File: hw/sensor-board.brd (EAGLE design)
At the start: 50 x 40 mm, 51 parts, among them U1 LT1762EMS8-3.3PBF, U2 ULN2003LVPWR, U3 ULN2003LVPWR, U4 PCA9685PW, U5 AT42QT1070-SSU, X1 MOLEX-501953-0407, X2 MOLEX-501953-0407

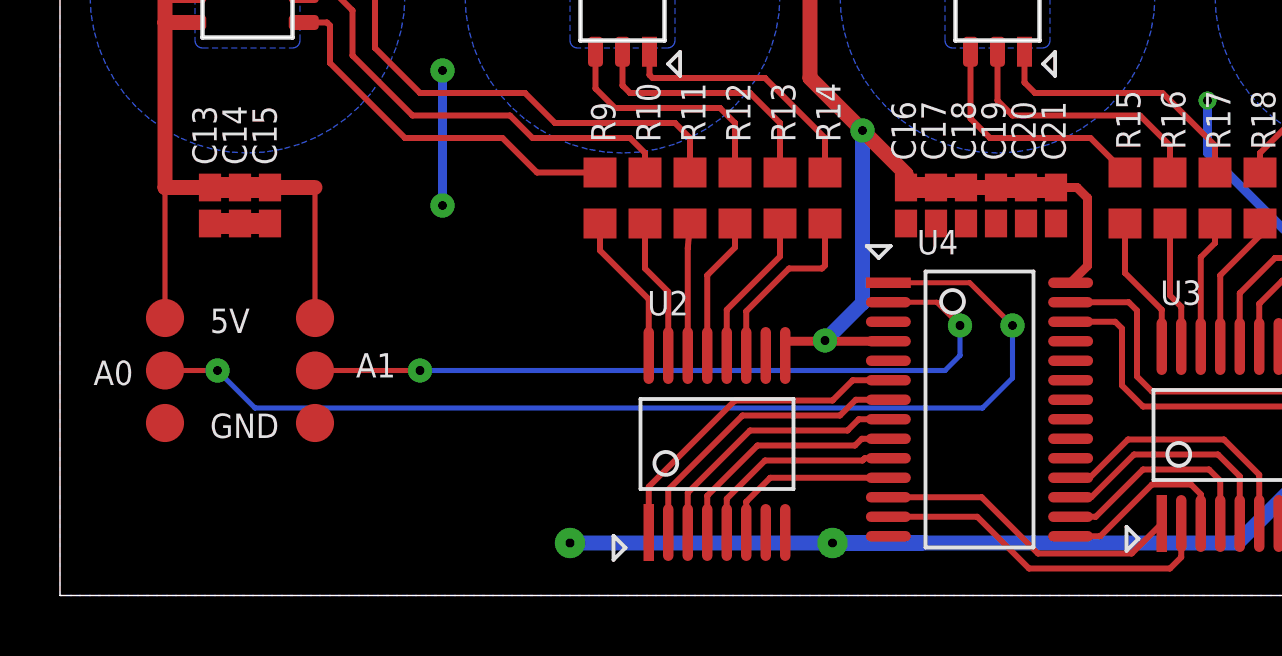
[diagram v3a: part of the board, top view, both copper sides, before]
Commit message: Switched VDD of LED PWM driver to 3.3V.
Added an LDO to generate VDD for LED PWM driver.
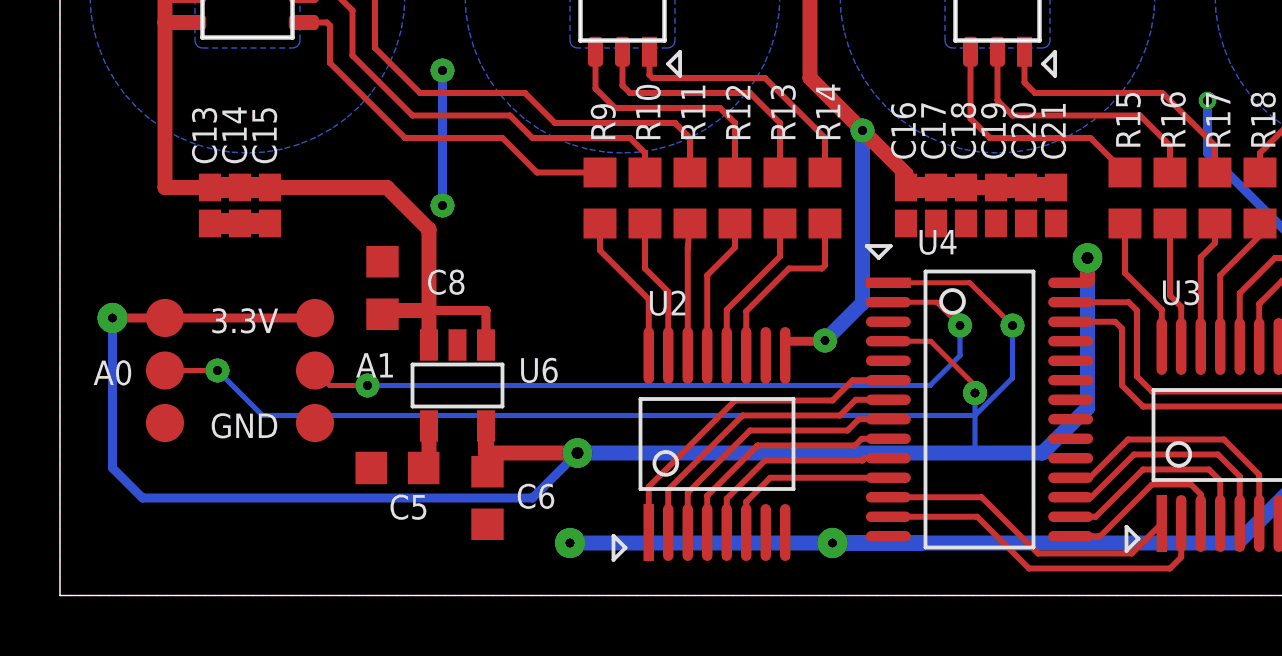
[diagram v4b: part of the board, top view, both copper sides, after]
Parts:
- added C5: 0.01uF 25V, rcl:C0603K
- added C6, C8: 1uF 25V, rcl:C0603K
- added U6: TPS730XX, vreg:SOT23-5
- renumbered 5V to 3.3V
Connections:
- new net N$1: C5.1, U6.4
- new net N$9: 3.3V.TP, C6.2, TP1.TP, U4.28, U4.4, U6.5
- net GND: now also C5.2, C6.1, C8.2, U2.7, U3.7, U6.2
- net VDD_5: now also C8.1, U6.1, U6.3; no longer 3.3V.TP, TP1.TP, U4.28, U4.4
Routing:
- net N$9: track 0.00 -> 65.8 mm, vias 0 -> 4
- net VDD_5: track 150.3 -> 148.1 mm
- net N$1: track 0.00 -> 1.58 mm
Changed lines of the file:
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@@
 <attribute name="VALUE" x="4.262" y="8.615" size="0.0254" layer="27" rot="R90"/>
 </element>
-<element name="5V" library="testpad" package="B1,27" value="TPB1,27" x="8.5" y="9.25" smashed="yes" rot="R90">
+<element name="3.3V" library="testpad" package="B1,27" value="TPB1,27" x="8.5" y="9.25" smashed="yes" rot="R90">
 <attribute name="TP_SIGNAL_NAME" value="" x="10.405" y="8.615" size="1" layer="37" rot="R90"/>
 <attribute name="NAME" x="5" y="8.75" size="0.8128" layer="25" font="vector" ratio="10"/>
@@
 <attribute name="ELEMENT14_URL" value="http://sg.element14.com/jsp/search/productdetail.jsp?sku=1799462" x="10" y="29.25" size="0.8128" layer="27" display="off"/>
 <attribute name="MFR_PART" value="RC0603JR-1047KL" x="10" y="29.25" size="0.8128" layer="27" display="off"/>
+</element>
+<element name="U6" library="vreg" package="SOT23-5" value="TPS730XX" x="13.25" y="7" smashed="yes" rot="R180">
+<attribute name="NAME" x="16.655" y="7.91" size="0.8128" layer="25" rot="R180"/>
+<attribute name="VALUE" x="15.155" y="10.175" size="0.8128" layer="27" rot="R180"/>
+</element>
+<element name="C5" library="rcl" package="C0603K" value="0.01uF 25V" x="11.25" y="4.25" smashed="yes" rot="R180">
+<attribute name="ELEMENT14_URL" value="http://sg.element14.com/jsp/search/productdetail.jsp?sku=1692285" x="11.25" y="4.25" size="0.8128" layer="27" rot="R180" display="off"/>
+<attribute name="MFR_PART" value="C0402C103J3RACTU" x="11.25" y="4.25" size="0.8128" layer="27" rot="R180" display="off"/>
+<attribute name="NAME" x="12.3" y="3.35" size="0.8128" layer="25" rot="R180"/>
+<attribute name="VALUE" x="12.05" y="5.9" size="1.016" layer="27" rot="R180"/>
+</element>
+<element name="C6" library="rcl" package="C0603K" value="1uF 25V" x="14.25" y="3.25" smashed="yes" rot="R90">
+<attribute name="ELEMENT14_URL" value="http://sg.element14.com/jsp/search/productdetail.jsp?sku=2146156" x="14.25" y="3.25" size="0.8128" layer="27" rot="R90" display="off"/>
+<attribute name="MFR_PART" value="C1608X7R1C105K080AC" x="14.25" y="3.25" size="0.8128" layer="27" rot="R90" display="off"/>
+<attribute name="NAME" x="15.2" y="2.9" size="0.8128" layer="25"/>
+<attribute name="VALUE" x="15.9" y="2.45" size="1.016" layer="27" rot="R90"/>
+</element>
+<element name="C8" library="rcl" package="C0603K" value="1uF 25V" x="10.75" y="10.25" smashed="yes" rot="R90">
+<attribute name="ELEMENT14_URL" value="http://sg.element14.com/jsp/search/productdetail.jsp?sku=2146156" x="10.75" y="10.25" size="0.8128" layer="27" rot="R90" display="off"/>
+<attribute name="MFR_PART" value="C1608X7R1C105K080AC" x="10.75" y="10.25" size="0.8128" layer="27" rot="R90" display="off"/>
+<attribute name="NAME" x="13.55" y="10.85" size="0.8128" layer="25" rot="R180"/>
+<attribute name="VALUE" x="12.4" y="9.45" size="1.016" layer="27" rot="R90"/>
 </element>
 </elements>
@@
 <contactref element="U1" pad="8"/>
 <contactref element="C3" pad="1"/>
-<contactref element="U4" pad="28"/>
 <contactref element="C13" pad="2"/>
 <contactref element="X2" pad="1"/>
@@
 <wire x1="44.5" y1="13.6" x2="45.5" y2="13.6" width="0.5" layer="1"/>
 <wire x1="45.5" y1="13.6" x2="46.5" y2="13.6" width="0.5" layer="1"/>
-<contactref element="U4" pad="4"/>
-<wire x1="27.6125" y1="8.475" x2="25.475" y2="8.475" width="0.3" layer="1"/>
 <wire x1="24.175" y1="8.475" x2="24.175" y2="8" width="0.2" layer="1"/>
 <wire x1="12.9" y1="31.025" x2="13.775" y2="31.025" width="0.3" layer="1"/>
@@
 <wire x1="13.75" y1="34.25" x2="12.9" y2="33.4" width="0.3" layer="1"/>
 <contactref element="X1" pad="1"/>
-<contactref element="TP1" pad="TP"/>
-<contactref element="5V" pad="TP"/>
 <wire x1="47.75" y1="22.75" x2="47.75" y2="13.5" width="0.5" layer="1"/>
 <wire x1="47.75" y1="13.5" x2="47.75" y2="11.75" width="0.5" layer="1"/>
@@
 <wire x1="24.175" y1="8.475" x2="25.475" y2="8.475" width="0.3" layer="1"/>
 <wire x1="25.475" y1="8.475" x2="25.5" y2="8.5" width="0.3" layer="1"/>
-<wire x1="33.2" y1="13.6" x2="33.9" y2="13.6" width="0.3" layer="1"/>
-<wire x1="33.9" y1="13.6" x2="34.25" y2="13.25" width="0.3" layer="1"/>
-<wire x1="34.25" y1="13.25" x2="34.25" y2="10.9875" width="0.3" layer="1"/>
-<wire x1="34.25" y1="10.9875" x2="33.6875" y2="10.425" width="0.3" layer="1"/>
-<wire x1="3.5" y1="13.6" x2="3.5" y2="9.25" width="0.17" layer="1"/>
-<wire x1="8.5" y1="9.25" x2="8.5" y2="13.6" width="0.17" layer="1"/>
 <wire x1="3.5" y1="13.6" x2="5" y2="13.6" width="0.5" layer="1"/>
-<wire x1="8.5" y1="13.6" x2="7" y2="13.6" width="0.5" layer="1"/>
 <wire x1="25" y1="17.25" x2="25" y2="22.75" width="0.5" layer="1"/>
+<contactref element="U6" pad="1"/>
+<contactref element="U6" pad="3"/>
+<wire x1="7" y1="13.6" x2="10.9" y2="13.6" width="0.5" layer="1"/>
+<wire x1="10.9" y1="13.6" x2="12.3" y2="12.2" width="0.5" layer="1"/>
+<wire x1="12.3" y1="12.2" x2="12.3" y2="9.5" width="0.5" layer="1"/>
+<wire x1="12.3" y1="9.5" x2="12.3" y2="8.35" width="0.5" layer="1"/>
+<wire x1="14.2" y1="8.35" x2="14.2" y2="9.5" width="0.3048" layer="1"/>
+<wire x1="14.2" y1="9.5" x2="12.3" y2="9.5" width="0.3048" layer="1"/>
+<contactref element="C8" pad="1"/>
+<wire x1="10.75" y1="9.375" x2="10.75" y2="9.5" width="0.5" layer="1"/>
+<wire x1="10.75" y1="9.5" x2="12.3" y2="9.5" width="0.5" layer="1"/>
 <wire x1="18" y1="22.75" x2="13.775" y2="31.025" width="0" layer="19" extent="1-1"/>
 </signal>
@@
 <contactref element="X2" pad="5"/>
 <contactref element="PWR" pad="2"/>
+<contactref element="U6" pad="2"/>
+<contactref element="C5" pad="2"/>
+<contactref element="C6" pad="1"/>
+<contactref element="U2" pad="7"/>
+<contactref element="U3" pad="7"/>
+<contactref element="C8" pad="2"/>
 </signal>
 <signal name="VDD_3_3">
@@
 <via x="31.75" y="9" extent="1-16" drill="0.3" diameter="0.8128"/>
 <wire x1="31.75" y1="9" x2="31.75" y2="7.25" width="0.17" layer="16"/>
-<wire x1="31.75" y1="7.25" x2="30.75" y2="6.25" width="0.17" layer="16"/>
-<wire x1="30.75" y1="6.25" x2="6.5" y2="6.25" width="0.17" layer="16"/>
-<wire x1="6.5" y1="6.25" x2="5.25" y2="7.5" width="0.17" layer="16"/>
 <via x="5.25" y="7.5" extent="1-16" drill="0.3" diameter="0.8128"/>
+<wire x1="31.75" y1="7.25" x2="30.5" y2="6" width="0.17" layer="16"/>
+<wire x1="30.5" y1="6" x2="6.75" y2="6" width="0.17" layer="16"/>
+<wire x1="6.75" y1="6" x2="5.25" y2="7.5" width="0.17" layer="16"/>
 </signal>
 <signal name="N$7">
@@
 <wire x1="29.225" y1="9.775" x2="30" y2="9" width="0.17" layer="1"/>
 <via x="30" y="9" extent="1-16" drill="0.3" diameter="0.8128"/>
-<wire x1="30" y1="9" x2="30" y2="8" width="0.17" layer="16"/>
-<wire x1="30" y1="8" x2="29.5" y2="7.5" width="0.17" layer="16"/>
-<wire x1="29.5" y1="7.5" x2="12" y2="7.5" width="0.17" layer="16"/>
-<via x="12" y="7.5" extent="1-16" drill="0.3" diameter="0.8128"/>
-<wire x1="12" y1="7.5" x2="8.5" y2="7.5" width="0.17" layer="1"/>
+<via x="10.25" y="7" extent="1-16" drill="0.3" diameter="0.8128"/>
+<wire x1="10.25" y1="7" x2="29" y2="7" width="0.17" layer="16"/>
+<wire x1="29" y1="7" x2="30" y2="8" width="0.17" layer="16"/>
+<wire x1="30" y1="8" x2="30" y2="9" width="0.17" layer="16"/>
+<wire x1="10.25" y1="7" x2="9" y2="7" width="0.17" layer="1"/>
+<wire x1="9" y1="7" x2="8.5" y2="7.5" width="0.17" layer="1"/>
+</signal>
+<signal name="N$9">
+<contactref element="U4" pad="4"/>
+<contactref element="U4" pad="28"/>
+<contactref element="U6" pad="5"/>
+<contactref element="TP1" pad="TP"/>
+<contactref element="3.3V" pad="TP"/>
+<contactref element="C6" pad="2"/>
+<wire x1="14.2" y1="5.65" x2="14.2" y2="4.125" width="0.5" layer="1"/>
+<wire x1="14.2" y1="4.125" x2="14.25" y2="4.125" width="0.5" layer="1"/>
+<wire x1="14.2" y1="5.65" x2="14.2" y2="4.75" width="0.5" layer="1"/>
+<wire x1="14.2" y1="4.75" x2="17.25" y2="4.75" width="0.5" layer="1"/>
+<via x="17.25" y="4.75" extent="1-16" drill="0.4" diameter="1"/>
+<wire x1="17.25" y1="4.75" x2="32.75" y2="4.75" width="0.5" layer="16"/>
+<wire x1="32.75" y1="4.75" x2="34.25" y2="6.25" width="0.5" layer="16"/>
+<wire x1="34.25" y1="6.25" x2="34.25" y2="11.25" width="0.5" layer="16"/>
+<via x="34.25" y="11.25" extent="1-16" drill="0.4" diameter="1"/>
+<wire x1="34.25" y1="11.25" x2="34.25" y2="10.5" width="0.5" layer="1"/>
+<wire x1="34.25" y1="10.5" x2="34.175" y2="10.425" width="0.3" layer="1"/>
+<wire x1="34.175" y1="10.425" x2="33.6875" y2="10.425" width="0.3" layer="1"/>
+<wire x1="17.25" y1="4.75" x2="15.75" y2="3.25" width="0.3" layer="16"/>
+<wire x1="15.75" y1="3.25" x2="2.75" y2="3.25" width="0.3" layer="16"/>
+<wire x1="2.75" y1="3.25" x2="1.75" y2="4.25" width="0.3" layer="16"/>
+<wire x1="1.75" y1="4.25" x2="1.75" y2="9.25" width="0.3" layer="16"/>
+<wire x1="1.75" y1="9.25" x2="3.5" y2="9.25" width="0.3" layer="1"/>
+<wire x1="3.5" y1="9.25" x2="8.5" y2="9.25" width="0.3" layer="1"/>
+<via x="1.75" y="9.25" extent="1-16" drill="0.3" diameter="1.016"/>
+<wire x1="32.75" y1="4.75" x2="30.5" y2="4.75" width="0.17" layer="16"/>
+<wire x1="30.5" y1="4.75" x2="30.5" y2="6.75" width="0.17" layer="16"/>
+<via x="30.5" y="6.75" extent="1-16" drill="0.3" diameter="0.8128"/>
+<wire x1="30.5" y1="6.75" x2="30.5" y2="7" width="0.17" layer="1"/>
+<wire x1="30.5" y1="7" x2="29.025" y2="8.475" width="0.17" layer="1"/>
+<wire x1="27.6125" y1="8.475" x2="29.025" y2="8.475" width="0.17" layer="1"/>
+</signal>
+<signal name="N$1">
+<contactref element="U6" pad="4"/>
+<contactref element="C5" pad="1"/>
+<wire x1="12.3" y1="5.65" x2="12.3" y2="4.25" width="0.5" layer="1"/>
+<wire x1="12.3" y1="4.25" x2="12.125" y2="4.25" width="0.5" layer="1"/>
 </signal>
 </signals>
